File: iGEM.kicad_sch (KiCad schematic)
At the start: 62 parts, among them IC1 TMCS1107A1BQDRQ1, IC2 MCP4642-502E_UN, IC3 SN74LVC2G08IDCTRQ1, IC4 NLSX4373DR2G, J1 COIL, J2 Conn_01x03, J3 Conn_01x02, J4 Conn_01x04, J5 Conn_01x03, J6 Conn_02x03_Odd_Even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

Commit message: updated to include programming power protection and cleanup
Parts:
- removed D10: 1N5817, Diode_THT:D_DO-41_SOD81_P10.16mm_Horizontal, symbol Diode:1N5817
- added D10: B130-E3, Diode_SMD:D_SMA, symbol Diode:B130-E3
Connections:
- net +5V: now also D10.1 (K)
- net at J6.2 (Pin_2): now also D10.2 (A)
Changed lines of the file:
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@@
     (pin "1")
+  )
+  (symbol (lib_id "Diode:B130-E3") (at 92.456 160.274 180) (unit 1)
+    (in_bom yes) (on_board yes) (fields_autoplaced)
+    (property "Reference" "D10" (id 0) (at 92.7735 153.416 0))
+    (property "Value" "B130-E3" (id 1) (at 92.7735 155.956 0))
+    (property "Footprint" "Diode_SMD:D_SMA" (id 2) (at 92.456 155.829 0)
+      (effects (font (size 1.27 1.27)) hide)
+    )
+    (property "Datasheet" "http://www.vishay.com/docs/88946/b120.pdf" (id 3) (at 92.456 160.274 0)
+      (effects (font (size 1.27 1.27)) hide)
+    )
+    (property "DigiKey" "B130-E3/5ATGICT-ND" (id 4) (at 92.456 160.274 0)
+      (effects (font (size 1.27 1.27)) hide)
+    )
+    (pin "1")
+    (pin "2")
   )
   (symbol (lib_id "Device:D_Schottky") (at 162.306 68.834 270) (unit 1)
@@
     (pin "6")
   )
+  (symbol (lib_id "power:VCC") (at 253.238 38.608 180) (unit 1)
+    (in_bom yes) (on_board yes) (fields_autoplaced)
+    (property "Reference" "#PWR042" (id 0) (at 253.238 34.798 0)
+      (effects (font (size 1.27 1.27)) hide)
+    )
+    (property "Value" "VCC" (id 1) (at 254.762 39.8779 0)
+      (effects (font (size 1.27 1.27)) (justify right))
+    )
+    (property "Footprint" "" (id 2) (at 253.238 38.608 0)
+      (effects (font (size 1.27 1.27)) hide)
+    )
+    (property "Datasheet" "" (id 3) (at 253.238 38.608 0)
+      (effects (font (size 1.27 1.27)) hide)
+    )
+    (pin "1")
+  )
   (symbol (lib_id "power:GND") (at 102.108 134.112 0) (unit 1)
     (in_bom yes) (on_board yes)
@@
     )
     (property "Datasheet" "~" (id 3) (at 220.98 21.971 0)
+      (effects (font (size 1.27 1.27)) hide)
+    )
+    (pin "1")
+  )
+  (symbol (lib_id "power:PWR_FLAG") (at 253.238 38.608 0) (unit 1)
+    (in_bom yes) (on_board yes) (fields_autoplaced)
+    (property "Reference" "#FLG01" (id 0) (at 253.238 36.703 0)
+      (effects (font (size 1.27 1.27)) hide)
+    )
+    (property "Value" "PWR_FLAG" (id 1) (at 253.238 32.893 0))
+    (property "Footprint" "" (id 2) (at 253.238 38.608 0)
+      (effects (font (size 1.27 1.27)) hide)
+    )
+    (property "Datasheet" "~" (id 3) (at 253.238 38.608 0)
       (effects (font (size 1.27 1.27)) hide)
     )
@@
     (pin "1")
   )
-  (symbol (lib_id "Diode:1N5817") (at 92.456 160.274 180) (unit 1)
-    (in_bom yes) (on_board yes) (fields_autoplaced)
-    (property "Reference" "D10" (id 0) (at 92.7735 153.67 0))
-    (property "Value" "1N5817" (id 1) (at 92.7735 156.21 0))
-    (property "Footprint" "Diode_THT:D_DO-41_SOD81_P10.16mm_Horizontal" (id 2) (at 92.456 155.829 0)
-      (effects (font (size 1.27 1.27)) hide)
-    )
-    (property "Datasheet" "http://www.vishay.com/docs/88525/1n5817.pdf" (id 3) (at 92.456 160.274 0)
-      (effects (font (size 1.27 1.27)) hide)
-    )
-    (property "DigiKey" "1N5817DICT-ND" (id 4) (at 92.456 160.274 0)
-      (effects (font (size 1.27 1.27)) hide)
-    )
-    (pin "1")
-    (pin "2")
-  )
   (symbol (lib_id "power:GND") (at 263.398 32.258 0) (unit 1)
     (in_bom yes) (on_board yes) (fields_autoplaced)
@@
   )
   (symbol_instances
+    (path "/d8dc518b-4cce-4e39-ae1b-d769618ae758"
+      (reference "#FLG01") (unit 1) (value "PWR_FLAG") (footprint "")
+    )
     (path "/283ccf20-375b-4aba-aadb-32b7acd18bdf"
       (reference "#FLG0101") (unit 1) (value "PWR_FLAG") (footprint "")
@@
       (reference "#PWR041") (unit 1) (value "GND") (footprint "")
     )
+    (path "/6ada2165-6b2a-4f4a-8f36-ad0fec66b078"
+      (reference "#PWR042") (unit 1) (value "VCC") (footprint "")
+    )
     (path "/2a7c0bd4-8344-40d3-a39f-5f0c146620d7"
       (reference "#PWR045") (unit 1) (value "+5V") (footprint "")
@@
       (reference "D9") (unit 1) (value "SB2060") (footprint "Diode_THT:D_DO-201AD_P12.70mm_Horizontal")
     )
-    (path "/f0c1cbd6-ee7e-45ca-9989-3cbb75ada46d"
-      (reference "D10") (unit 1) (value "1N5817") (footprint "Diode_THT:D_DO-41_SOD81_P10.16mm_Horizontal")
+    (path "/36c18202-752c-4d1f-a3af-6d5a088ec0d3"
+      (reference "D10") (unit 1) (value "B130-E3") (footprint "Diode_SMD:D_SMA")
     )
     (path "/eadcb800-30ab-4a2d-bc96-28b421a136a3"

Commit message: Replace out of stock Stemma QT header
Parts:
- J4: footprint Connector_JST:JST_SH_SM04B-SRSS-TB_1x04-1MP_P1.00mm_Horizontal -> Connector_JST:JST_XH_B4B-XH-A_1x04_P2.50mm_Vertical; DigiKey (none) -> 455-2249-ND
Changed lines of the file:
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@@
       (effects (font (size 1.27 1.27)) (justify left))
     )
-    (property "Footprint" "Connector_JST:JST_SH_SM04B-SRSS-TB_1x04-1MP_P1.00mm_Horizontal" (id 2) (at 267.716 48.514 0)
+    (property "Footprint" "Connector_JST:JST_XH_B4B-XH-A_1x04_P2.50mm_Vertical" (id 2) (at 267.716 48.514 0)
       (effects (font (size 1.27 1.27)) hide)
     )
     (property "Datasheet" "~" (id 3) (at 267.716 48.514 0)
+      (effects (font (size 1.27 1.27)) hide)
+    )
+    (property "DigiKey" "455-2249-ND" (id 4) (at 267.716 48.514 0)
       (effects (font (size 1.27 1.27)) hide)
     )
@@
     )
     (path "/c114912b-506d-46cd-9190-0782b54aa74f"
-      (reference "J4") (unit 1) (value "Conn_01x04") (footprint "Connector_JST:JST_SH_SM04B-SRSS-TB_1x04-1MP_P1.00mm_Horizontal")
+      (reference "J4") (unit 1) (value "Conn_01x04") (footprint "Connector_JST:JST_XH_B4B-XH-A_1x04_P2.50mm_Vertical")
     )
     (path "/9b2f8761-bd4e-4c91-9a1d-8ce4be0ce7a3"

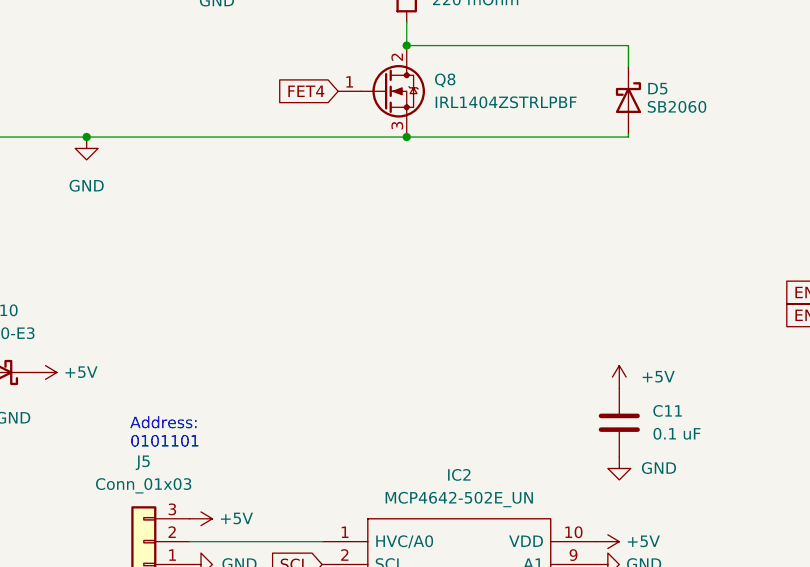
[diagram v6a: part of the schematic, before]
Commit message: Adding QTPY RP2040 as a backup if ATTiny412 does not work
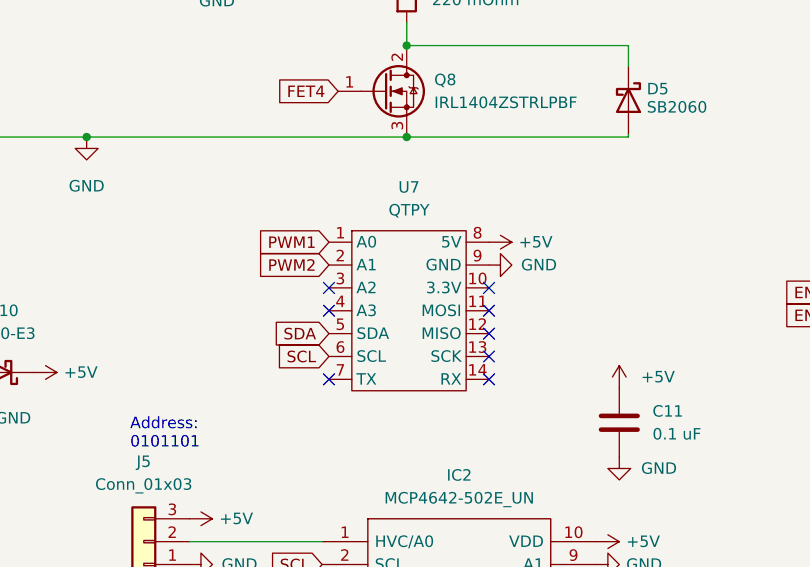
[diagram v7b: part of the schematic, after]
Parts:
- added U7: QTPY, QTPY:QTPY-RP2040, symbol QTPY:QTPY
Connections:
- net +5V: now also U7.8 (5V)
- net GND: now also U7.9 (GND)
- net PWM1: now also U7.1 (A0)
- net PWM2: now also U7.2 (A1)
- net SCL: now also U7.6 (SCL)
- net SDA: now also U7.5 (SDA)
- no-connect marks 7 -> 15
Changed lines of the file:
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@@
   (no_connect (at 236.093 24.638))
   (no_connect (at 243.84 24.765))
+  (no_connect (at 129.032 161.036))
+  (no_connect (at 129.032 153.416))
+  (no_connect (at 129.032 150.876))
+  (no_connect (at 146.812 150.876))
+  (no_connect (at 146.812 153.416))
+  (no_connect (at 146.812 155.956))
+  (no_connect (at 146.812 158.496))
+  (no_connect (at 146.812 161.036))
   (wire (pts (xy 113.538 179.07) (xy 128.27 179.07))
     (stroke (width 0) (type default) (color 0 0 0 0))
@@
     )
   )
+  (global_label "PWM2" (shape input) (at 129.032 148.336 180) (fields_autoplaced)
+    (effects (font (size 1.27 1.27)) (justify right))
+    (property "Intersheet References" "${INTERSHEET_REFS}" (id 0) (at 121.2365 148.4154 0)
+      (effects (font (size 1.27 1.27)) (justify right) hide)
+    )
+  )
   (global_label "DIR1" (shape input) (at 242.824 143.764 180) (fields_autoplaced)
     (effects (font (size 1.27 1.27)) (justify right))
@@
     )
   )
+  (global_label "SCL" (shape input) (at 129.032 158.496 180) (fields_autoplaced)
+    (effects (font (size 1.27 1.27)) (justify right))
+    (property "Intersheet References" "${INTERSHEET_REFS}" (id 0) (at 123.1113 158.4166 0)
+      (effects (font (size 1.27 1.27)) (justify right) hide)
+    )
+  )
   (global_label "FET2" (shape input) (at 263.144 146.304 0) (fields_autoplaced)
     (effects (font (size 1.27 1.27)) (justify left))
@@
     )
   )
+  (global_label "SDA" (shape input) (at 129.032 155.956 180) (fields_autoplaced)
+    (effects (font (size 1.27 1.27)) (justify right))
+    (property "Intersheet References" "${INTERSHEET_REFS}" (id 0) (at 123.0508 155.8766 0)
+      (effects (font (size 1.27 1.27)) (justify right) hide)
+    )
+  )
   (global_label "FET1" (shape input) (at 46.482 68.834 0) (fields_autoplaced)
     (effects (font (size 1.27 1.27)) (justify left))
@@
     )
   )
+  (global_label "PWM1" (shape input) (at 129.032 145.796 180) (fields_autoplaced)
+    (effects (font (size 1.27 1.27)) (justify right))
+    (property "Intersheet References" "${INTERSHEET_REFS}" (id 0) (at 121.2365 145.8754 0)
+      (effects (font (size 1.27 1.27)) (justify right) hide)
+    )
+  )
   (global_label "SDA-LOW" (shape input) (at 207.518 69.342 180) (fields_autoplaced)
     (effects (font (size 1.27 1.27)) (justify right))
@@
     (pin "1")
   )
+  (symbol (lib_id "QTPY:QTPY") (at 137.922 153.416 0) (unit 1)
+    (in_bom yes) (on_board yes) (fields_autoplaced)
+    (property "Reference" "U7" (id 0) (at 137.922 139.7 0))
+    (property "Value" "QTPY" (id 1) (at 137.922 142.24 0))
+    (property "Footprint" "QTPY:QTPY-RP2040" (id 2) (at 137.922 153.416 0)
+      (effects (font (size 1.27 1.27)) hide)
+    )
+    (property "Datasheet" "" (id 3) (at 137.922 153.416 0)
+      (effects (font (size 1.27 1.27)) hide)
+    )
+    (pin "1")
+    (pin "10")
+    (pin "11")
+    (pin "12")
+    (pin "13")
+    (pin "14")
+    (pin "2")
+    (pin "3")
+    (pin "4")
+    (pin "5")
+    (pin "6")
+    (pin "7")
+    (pin "8")
+    (pin "9")
+  )
   (symbol (lib_id "power:VCC") (at 207.518 66.802 90) (unit 1)
     (in_bom yes) (on_board yes) (fields_autoplaced)
@@
     (pin "2")
   )
+  (symbol (lib_id "power:+5V") (at 146.812 145.796 270) (unit 1)
+    (in_bom yes) (on_board yes) (fields_autoplaced)
+    (property "Reference" "#PWR0135" (id 0) (at 143.002 145.796 0)
+      (effects (font (size 1.27 1.27)) hide)
+    )
+    (property "Value" "+5V" (id 1) (at 150.114 145.7959 90)
+      (effects (font (size 1.27 1.27)) (justify left))
+    )
+    (property "Footprint" "" (id 2) (at 146.812 145.796 0)
+      (effects (font (size 1.27 1.27)) hide)
+    )
+    (property "Datasheet" "" (id 3) (at 146.812 145.796 0)
+      (effects (font (size 1.27 1.27)) hide)
+    )
+    (pin "1")
+  )
   (symbol (lib_id "dk_Logic-Gates-and-Inverters:SN74LVC1G04DBVR") (at 251.206 109.22 180) (unit 1)
     (in_bom yes) (on_board yes)
@@
     (pin "1")
   )
+  (symbol (lib_id "power:GND") (at 146.812 148.336 90) (unit 1)
+    (in_bom yes) (on_board yes) (fields_autoplaced)
+    (property "Reference" "#PWR0134" (id 0) (at 153.162 148.336 0)
+      (effects (font (size 1.27 1.27)) hide)
+    )
+    (property "Value" "GND" (id 1) (at 150.368 148.3359 90)
+      (effects (font (size 1.27 1.27)) (justify right))
+    )
+    (property "Footprint" "" (id 2) (at 146.812 148.336 0)
+      (effects (font (size 1.27 1.27)) hide)
+    )
+    (property "Datasheet" "" (id 3) (at 146.812 148.336 0)
+      (effects (font (size 1.27 1.27)) hide)
+    )
+    (pin "1")
+  )
   (symbol (lib_id "Device:LED") (at 182.626 45.466 270) (unit 1)
     (in_bom yes) (on_board yes) (fields_autoplaced)
@@
       (reference "#PWR0133") (unit 1) (value "GND") (footprint "")
     )
+    (path "/392f36d9-6b06-4048-bebc-d49935be0088"
+      (reference "#PWR0134") (unit 1) (value "GND") (footprint "")
+    )
+    (path "/2475768f-a2fa-4c93-ac7e-94cf43aef635"
+      (reference "#PWR0135") (unit 1) (value "+5V") (footprint "")
+    )
     (path "/0fbdd8b7-d3db-4cb1-9102-673f223a760c"
       (reference "C1") (unit 1) (value "0.1 uF") (footprint "Capacitor_SMD:C_0805_2012Metric_Pad1.18x1.45mm_HandSolder")
@@
       (reference "U6") (unit 1) (value "SN74LVC1G04DBVR") (footprint "digikey-footprints:SOT-753")
     )
+    (path "/1eed78e1-71a1-4454-8afa-da0bab06fe03"
+      (reference "U7") (unit 1) (value "QTPY") (footprint "QTPY:QTPY-RP2040")
+    )
   )

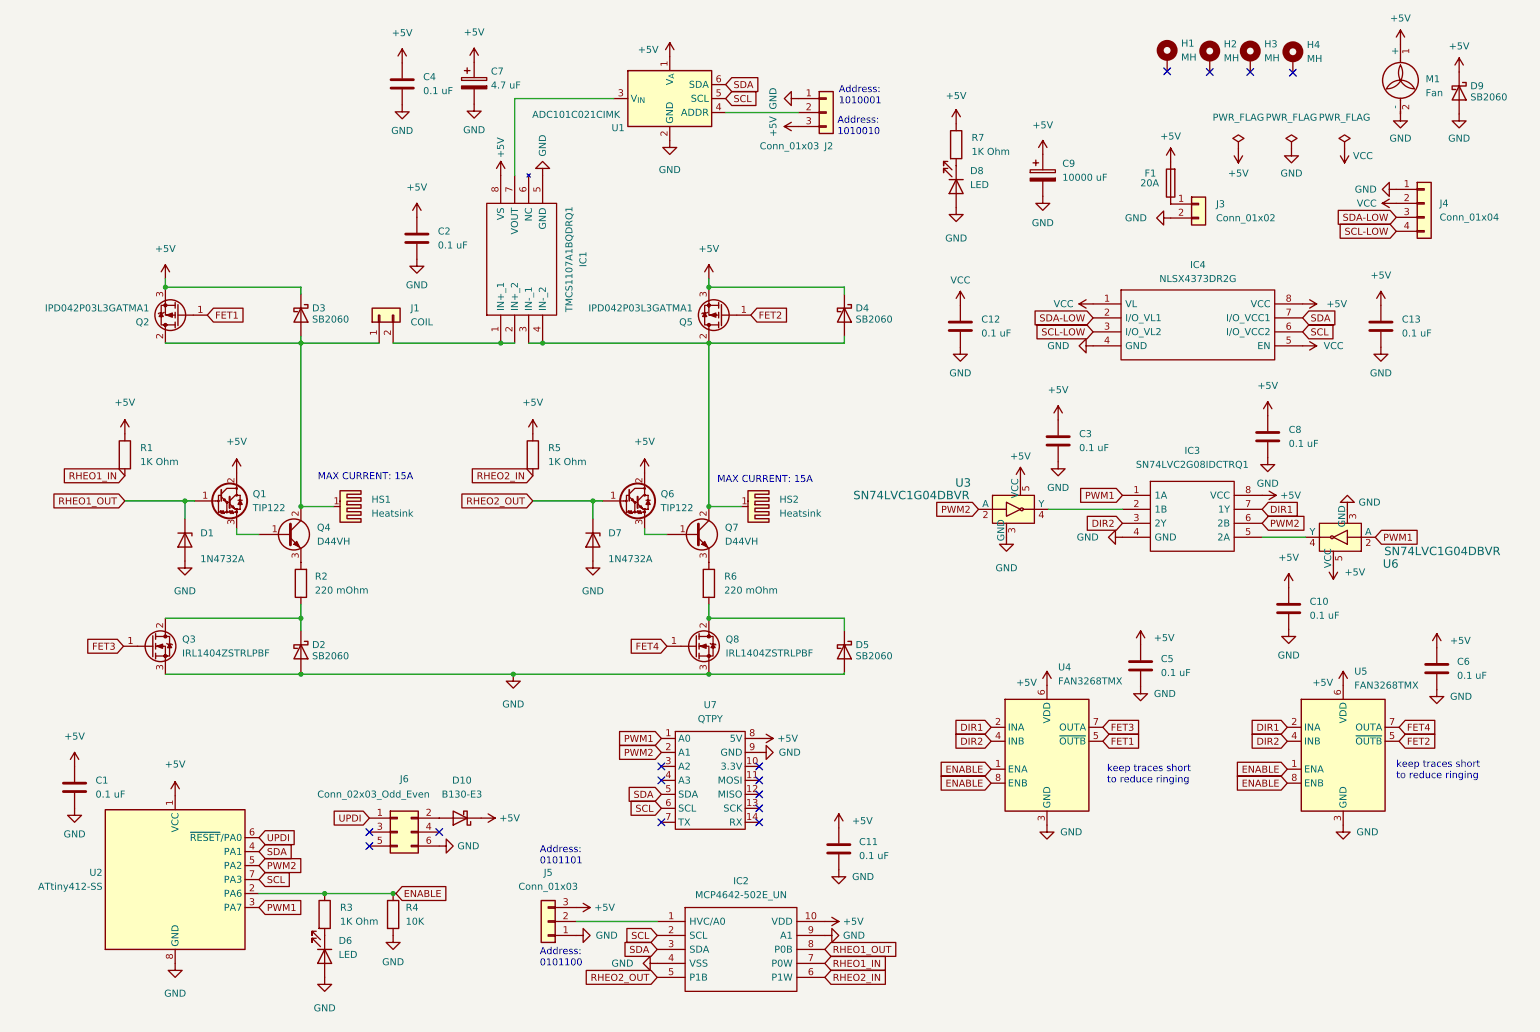
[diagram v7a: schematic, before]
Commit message: adding layout with RP2040 QTPY
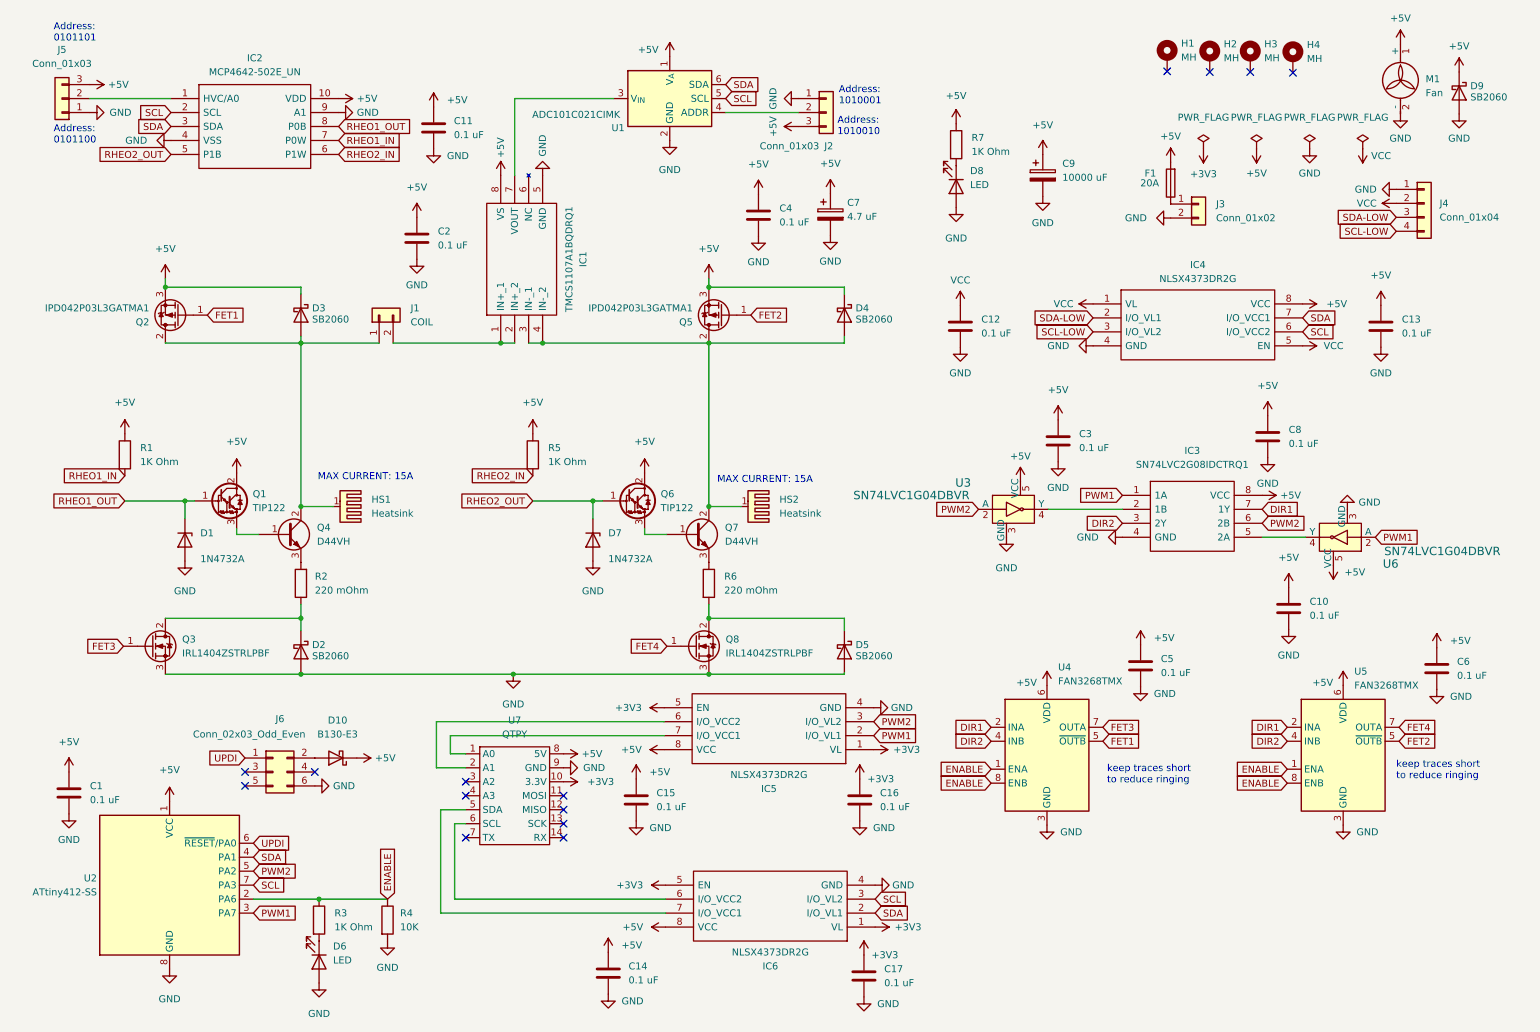
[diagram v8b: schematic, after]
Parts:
- added C14, C15, C16, C17: 0.1 uF, Capacitor_SMD:C_0805_2012Metric_Pad1.18x1.45mm_HandSolder, symbol Device:C
- added IC5, IC6: NLSX4373DR2G, Package_SO:SOIC-8_3.9x4.9mm_P1.27mm, symbol NLSX4373DR2G:NLSX4373DR2G
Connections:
- net +5V: now also C14.1, C15.1, IC5.8 (VCC), IC6.8 (VCC)
- net GND: now also C14.2, C15.2, C16.2, C17.2, IC5.4 (GND), IC6.4 (GND)
- net PWM1: now also IC5.2 (I/O_VL1); no longer U7.1 (A0)
- net PWM2: now also IC5.3 (I/O_VL2); no longer U7.2 (A1)
- net SCL: now also IC6.3 (I/O_VL2); no longer U7.6 (SCL)
- net SDA: now also IC6.2 (I/O_VL1); no longer U7.5 (SDA)
- net +3V3: now reaches U7.10 (3.3V)
- net +3V3: now also C16.1, C17.1, IC5.1 (VL), IC5.5 (EN), IC6.1 (VL), IC6.5 (EN)
- new net: IC6.6 (I/O_VCC2), U7.6 (SCL)
- new net: IC6.7 (I/O_VCC1), U7.5 (SDA)
- new net: IC5.7 (I/O_VCC1), U7.1 (A0)
- new net: IC5.6 (I/O_VCC2), U7.2 (A1)
- no-connect marks 15 -> 14
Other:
- moved on the sheet: C1, C11, C4, C7, D10, D6, IC2, J5, J6, R3, R4, U2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
